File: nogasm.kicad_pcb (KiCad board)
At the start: 2 copper layers, 76.2 x 76.2 mm, 57 parts, among them J1 DC Jack PJ-031DH 3.5mm, J2 DC Jack PRT-10811, Q1 BUK92150-55A, Q2 MMBT2222A, Q3 MMBT2222A, Q4 MMBT2222A, SW1 SW_DIP_x04, U1 WS2812B, U10 WS2812B, U11 WS2812B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

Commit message: refactoring
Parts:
- C13, C18: moved to F.Cu
- moved C18 4.14 mm to (133.6, 79.3), turned to 270 degrees
- moved C13 3.86 mm to (146.7, 79.5), turned to 270 degrees
- moved G*** 2.89 mm to (130.2, 78.1)
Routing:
- net GND: track 243.6 -> 259.8 mm, vias 21 -> 22
- net +5V: track 239.6 -> 236.0 mm
- net +12V: track 64.1 -> 65.3 mm, vias 0 -> 1

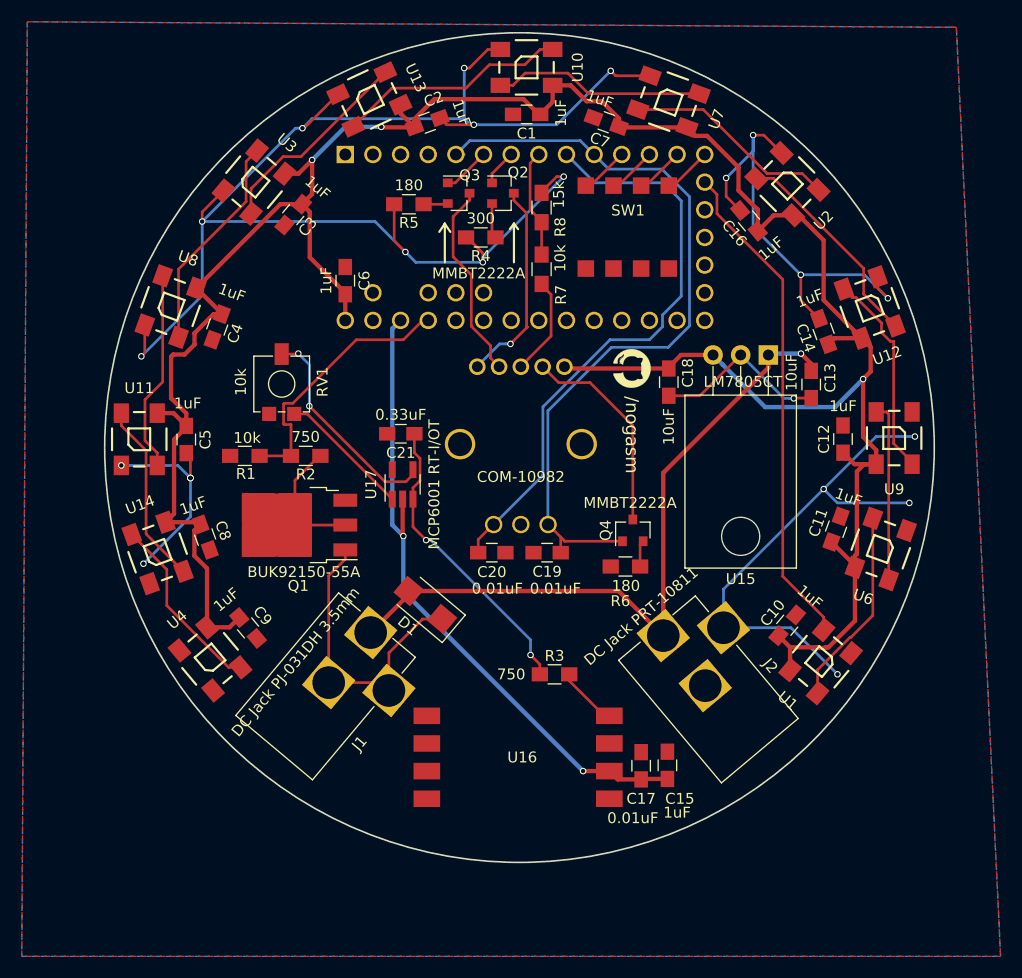
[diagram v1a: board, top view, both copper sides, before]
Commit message: adding proper barrel jack footprints and using them on the board
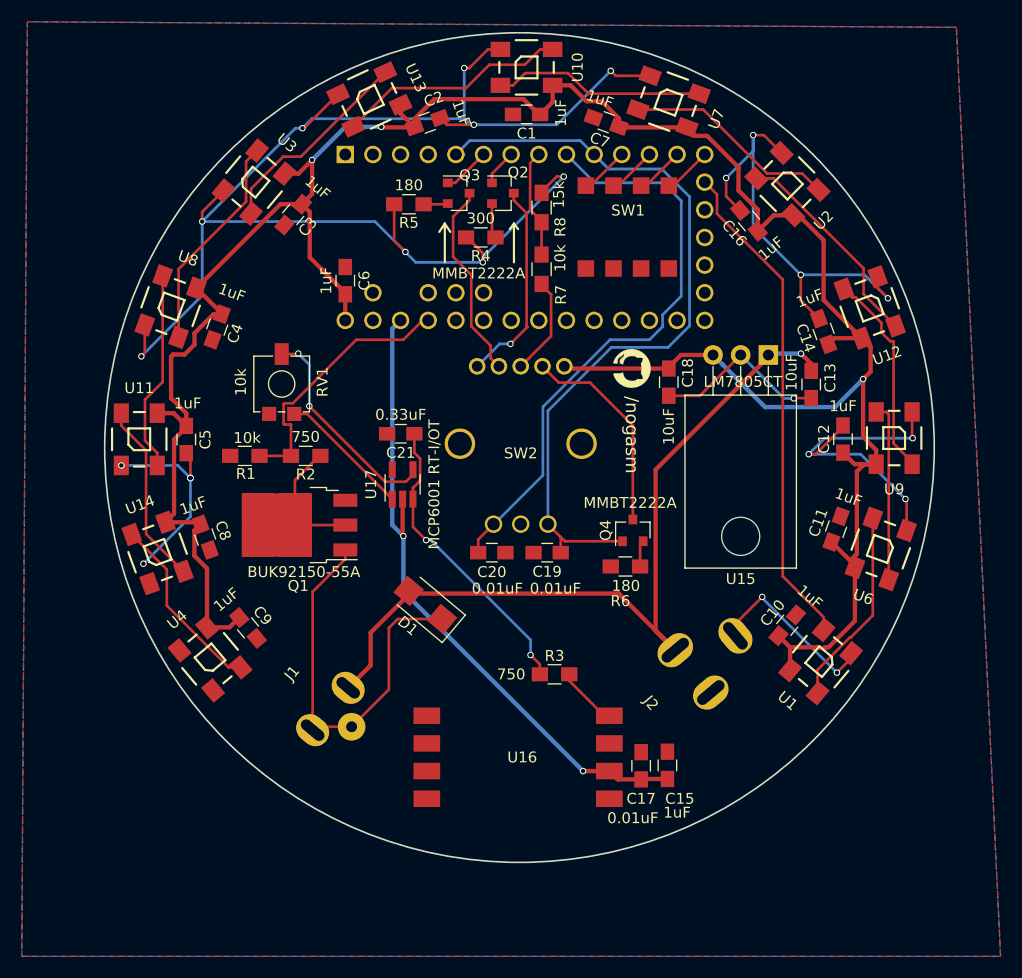
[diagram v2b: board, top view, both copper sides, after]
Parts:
- removed COM-10982: Rotary_Encoder_Switch_RGB, sma:COM-10982
- added SW2: Rotary_Encoder_Switch_RGB, nogasm:COM-10982, F.Cu at (120.0, 85.0)
- J1: footprint Connect:BARREL_JACK -> nogasm:Barreljack_3mm
- J2: footprint Connect:BARREL_JACK -> nogasm:Barreljack_5.4mm
- moved J1 7.93 mm to (102.5, 109.4), turned to 320 degrees
- moved J2 4.28 mm to (135.8, 105.9), turned to 40 degrees
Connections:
- U16 pad 1: (no net) -> Net-(U16-Pad1)
- U16 pad 5: (no net) -> Net-(U16-Pad5)
- U16 pad 6: (no net) -> Net-(U16-Pad6)
- U16 pad 7: (no net) -> Net-(U16-Pad7)
- U16 pad 8: (no net) -> Net-(U16-Pad8)
- U4 pad 2: (no net) -> Net-(U4-Pad2)
- U5 pad 1: (no net) -> Net-(U5-Pad1)
- U5 pad 16: (no net) -> Net-(U5-Pad16)
- U5 pad 17: (no net) -> Net-(U5-Pad17)
- U5 pad 18: (no net) -> Net-(U5-Pad18)
- U5 pad 19: (no net) -> Net-(U5-Pad19)
- U5 pad 2: (no net) -> Net-(U5-Pad2)
- U5 pad 20: (no net) -> Net-(U5-Pad20)
- U5 pad 21: (no net) -> Net-(U5-Pad21)
- U5 pad 22: (no net) -> /V_press
- U5 pad 23: (no net) -> Net-(U5-Pad23)
- U5 pad 24: (no net) -> Net-(U5-Pad24)
- U5 pad 25: (no net) -> Net-(U5-Pad25)
- U5 pad 26: (no net) -> Net-(U5-Pad26)
- U5 pad 27: (no net) -> Net-(U5-Pad27)
- U5 pad 28: (no net) -> Net-(U5-Pad28)
- U5 pad 29: (no net) -> Net-(U5-Pad29)
- U5 pad 3: (no net) -> Net-(U5-Pad3)
- U5 pad 34: (no net) -> Net-(U5-Pad34)
- U5 pad 35: (no net) -> Net-(U5-Pad35)
- U5 pad 36: (no net) -> Net-(U5-Pad36)
- U5 pad 37: (no net) -> Net-(U5-Pad37)
- U5 pad 4: (no net) -> Net-(U5-Pad4)
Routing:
- net +12V: track 65.3 -> 75.1 mm
- net Net-(D1-Pad1): track 30.3 -> 37.2 mm
- net GND: track 259.8 -> 259.4 mm, vias 22 -> 23

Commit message: fixing pad size of C13 and C 18. Fixing wrong D1 polarity
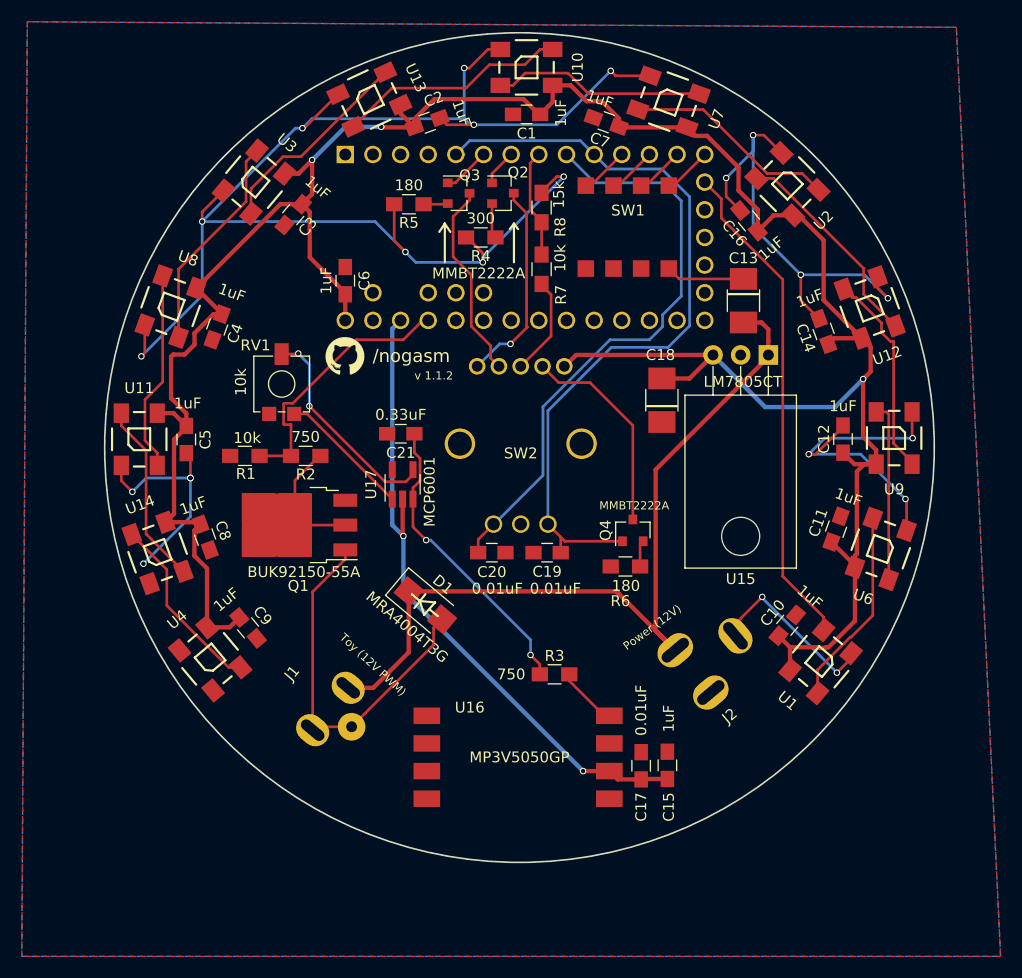
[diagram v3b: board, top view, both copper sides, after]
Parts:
- C13, C18: footprint Capacitors_SMD:C_0805_HandSoldering -> Capacitors_SMD:C_1210_HandSoldering
- J1: value DC Jack PJ-031DH 3.5mm -> 3mm Jack
- J2: value DC Jack PRT-10811 -> 5mm Jack
- U17: value MCP6001 RT-I/OT -> MCP6001
- moved G*** 26.4 mm to (103.9, 76.9), turned to 0 degrees
- moved C13 9.90 mm to (140.5, 71.8), turned to 90 degrees
- moved C18 1.78 mm to (133.0, 81.0)
- turned D1 to 320 degrees
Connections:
- D1 pad 1: Net-(D1-Pad1) -> +12V
- D1 pad 2: +12V -> Net-(D1-Pad2)
- J1 pad 2: Net-(D1-Pad1) -> Net-(D1-Pad2)
- J1 pad 3: Net-(D1-Pad1) -> Net-(D1-Pad2)
- Q1 pad 1: Net-(D1-Pad1) -> Net-(D1-Pad2)
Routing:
- net Net-(D1-Pad1): track 37.2 -> 0.00 mm
- net Net-(D1-Pad2): track 0.00 -> 34.8 mm
- net GND: track 259.4 -> 252.2 mm, vias 23 -> 22
- net +5V: track 236.0 -> 241.4 mm
- net +12V: track 75.1 -> 76.5 mm, vias 1 -> 0
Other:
- board text added: "Power (12V)"
- board text added: "Toy (12V PWM)"
- board text added: "v 1.1.2"

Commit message: fixing BUK pinout
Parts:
- J1: value 3mm Jack -> DC Jack PJ-031DH 3.5mm
- J2: value 5mm Jack -> DC Jack PRT-10811
- U17: value MCP6001 -> MCP6001 RT-I/OT
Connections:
- Q1 pad 1: Net-(D1-Pad2) -> Net-(Q1-Pad1)
- Q1 pad 2: Net-(Q1-Pad2) -> Net-(D1-Pad2)
- R2 pad 1: Net-(Q1-Pad2) -> Net-(Q1-Pad1)
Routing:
- net Net-(D1-Pad2): track 34.8 -> 47.7 mm, vias 0 -> 2
- net Net-(Q1-Pad1): track 0.00 -> 11.7 mm
- net Net-(Q1-Pad2): track 11.1 -> 0.00 mm
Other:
- board text added: "v 1.1.3"
- board text removed: "v 1.1.2"

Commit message: rerouting
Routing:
- net Net-(D1-Pad2): track 47.7 -> 42.2 mm, vias 2 -> 0
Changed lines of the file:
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@@
     (thickness 1.6)
     (drawings 19)
-    (tracks 455)
+    (tracks 451)
     (zones 0)
     (modules 57)
@@
   (segment (start 110.104 87.831) (end 109.453999 88.481001) (width 0.25) (layer F.Cu) (net 38) (status 10))
   (via (at 100.584 81.534) (size 0.6) (drill 0.4) (layers F.Cu B.Cu) (net 38))
-  (segment (start 99.261 96.213) (end 102.108 99.06) (width 0.25) (layer F.Cu) (net 67))
-  (segment (start 102.108 99.06) (end 105.664 102.616) (width 0.25) (layer F.Cu) (net 67))
+  (segment (start 95.911 93.987) (end 95.911 95.612) (width 0.25) (layer F.Cu) (net 67))
+  (segment (start 100.8888 109.748619) (end 100.8888 111.3028) (width 0.25) (layer F.Cu) (net 67))
+  (segment (start 95.911 95.612) (end 100.8888 100.5898) (width 0.25) (layer F.Cu) (net 67))
+  (segment (start 100.8888 100.5898) (end 100.8888 109.748619) (width 0.25) (layer F.Cu) (net 67))
   (segment (start 103.886 92.462) (end 103.386 92.462) (width 0.25) (layer F.Cu) (net 67))
-  (segment (start 112.776 106.172) (end 112.776 101.12315) (width 0.25) (layer F.Cu) (net 67))
-  (segment (start 105.664 102.616) (end 109.22 106.172) (width 0.25) (layer B.Cu) (net 67))
-  (via (at 112.776 106.172) (size 0.6) (drill 0.4) (layers F.Cu B.Cu) (net 67))
-  (segment (start 109.22 106.172) (end 112.776 106.172) (width 0.25) (layer B.Cu) (net 67))
-  (segment (start 99.261 93.987) (end 99.261 96.213) (width 0.25) (layer F.Cu) (net 67))
-  (via (at 105.664 102.616) (size 0.6) (drill 0.4) (layers F.Cu B.Cu) (net 67))
   (segment (start 103.886 92.462) (end 100.786 92.462) (width 0.25) (layer F.Cu) (net 67) (status 30))
   (segment (start 100.786 92.462) (end 99.261 90.937) (width 0.25) (layer F.Cu) (net 67) (status 30))

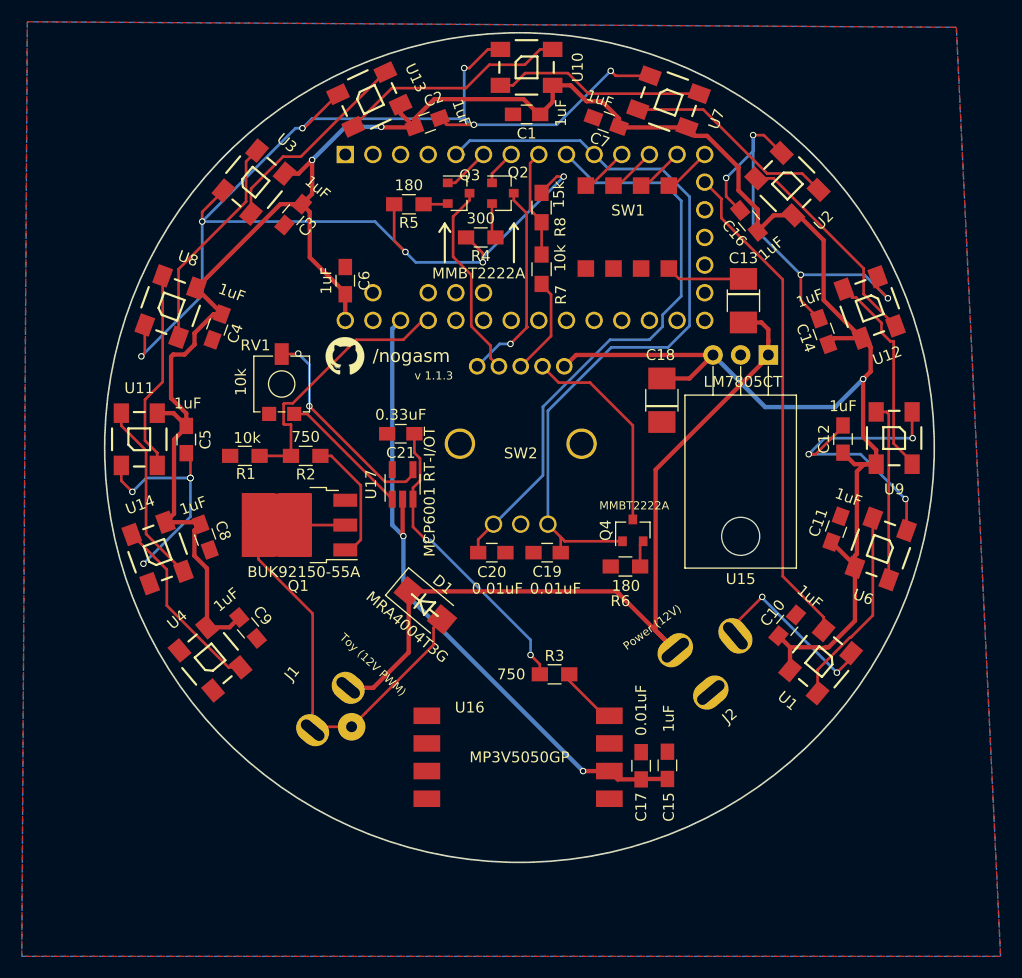
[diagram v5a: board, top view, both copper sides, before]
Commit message: fixing cap polarity marking on silkscreen
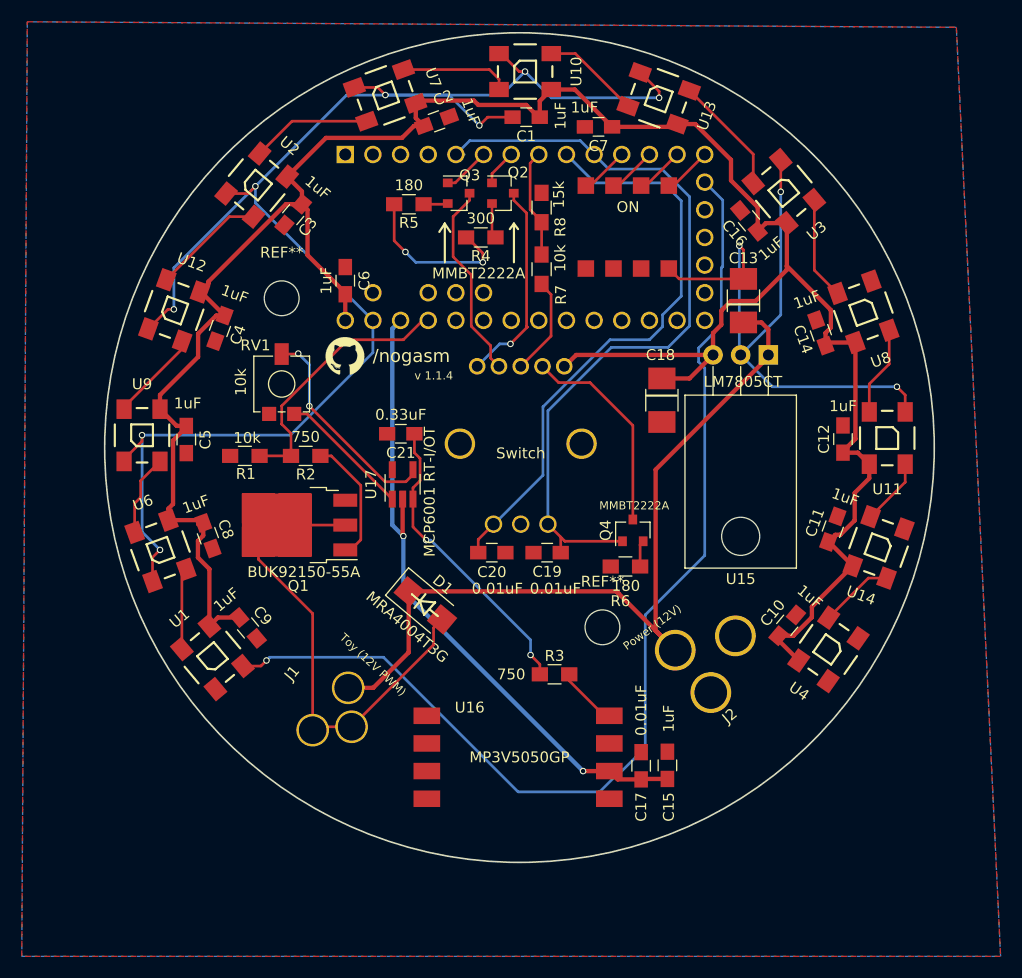
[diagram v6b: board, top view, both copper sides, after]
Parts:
- added REF**: MountingHole_3.2mm_M3, Mounting_Holes:MountingHole_3.2mm_M3, F.Cu at (127.5, 101.9)
- added REF**: MountingHole_3.2mm_M3, Mounting_Holes:MountingHole_3.2mm_M3, F.Cu at (98.0, 71.6)
- moved U9 69.1 mm to (85.2, 84.2), turned to 0 degrees
- moved U11 68.7 mm to (153.7, 84.5), turned to 180 degrees
- moved U14 66.2 mm to (152.9, 94.5), turned to 160 degrees
- moved U6 66.2 mm to (86.9, 94.8), turned to 20 degrees
- moved U12 63.9 mm to (88.2, 72.7), turned to 340 degrees
- moved U8 63.6 mm to (151.5, 72.9), turned to 200 degrees
- moved U4 56.8 mm to (148.3, 103.9), turned to 145 degrees
- moved U1 55.9 mm to (91.7, 104.6), turned to 40 degrees
- moved U2 48.8 mm to (95.7, 61.2), turned to 320 degrees
- moved U3 48.7 mm to (144.2, 61.8), turned to 220 degrees
- moved U13 26.6 mm to (132.7, 53.3), turned to 250 degrees
- moved U7 26.0 mm to (107.5, 53.0), turned to 290 degrees
- moved C2 0.87 mm to (112.3, 55.4)
- moved C7 0.83 mm to (127.1, 55.9), turned to 180.1 degrees
- moved U10 0.40 mm to (120.4, 50.8)
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- renumbered SW1 to ON, SW2 to Switch
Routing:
- net /5VIO: track 45.7 -> 100.1 mm, vias 0 -> 1
- net GND: track 252.2 -> 222.4 mm, vias 22 -> 13
- net +5V: track 241.4 -> 222.4 mm, vias 3 -> 0
- net Net-(U10-Pad2): track 21.3 -> 9.05 mm
- net Net-(U11-Pad2): track 16.9 -> 6.14 mm
- net Net-(U1-Pad2): track 18.2 -> 7.50 mm
- net Net-(U3-Pad2): track 20.1 -> 9.46 mm
- net Net-(U12-Pad4): track 19.1 -> 8.46 mm
- net Net-(U11-Pad4): track 18.6 -> 8.26 mm
- net Net-(U14-Pad2): track 17.0 -> 6.82 mm
- net Net-(U10-Pad4): track 19.5 -> 10.1 mm
- net Net-(U12-Pad2): track 19.8 -> 10.4 mm
- net Net-(U6-Pad2): track 16.4 -> 7.49 mm
- net Net-(U2-Pad2): track 19.7 -> 11.1 mm
- net Net-(U13-Pad2): track 19.1 -> 11.0 mm
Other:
- board text added: "v 1.1.4"
- board text removed: "v 1.1.3"

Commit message: removing silkscreen for drillholes and increasing version number
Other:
- board text added: "v 1.1.5"
- board text removed: "v 1.1.4"
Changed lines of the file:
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@@
     (descr "Mounting Hole 3.2mm, no annular, M3")
     (tags "mounting hole 3.2mm no annular m3")
-    (fp_text reference REF** (at 0 -4.2) (layer F.SilkS)
+    (fp_text reference REF** (at 0 -4.2) (layer F.Fab)
       (effects (font (size 1 1) (thickness 0.15)))
     )
@@
     (descr "Mounting Hole 3.2mm, no annular, M3")
     (tags "mounting hole 3.2mm no annular m3")
-    (fp_text reference REF** (at 0 -4.2) (layer F.SilkS)
+    (fp_text reference REF** (at 0 -4.2) (layer F.Fab)
       (effects (font (size 1 1) (thickness 0.15)))
     )
@@
     (effects (font (size 0.75 0.75) (thickness 0.15)))
   )
-  (gr_text "v 1.1.4" (at 112.014 78.74) (layer F.SilkS)
+  (gr_text "v 1.1.5" (at 112.014 78.74) (layer F.SilkS)
     (effects (font (size 0.75 0.75) (thickness 0.15)))
   )
